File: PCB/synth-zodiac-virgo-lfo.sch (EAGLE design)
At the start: 35 parts, among them Q10 PNP, Q11 NPN, Q9 PNP, U11 TL074A, U12 LM13700

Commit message: Almost ready for FAB.
Sagittarius was mis-spelled, renamed it.  Taurus is still WIP.
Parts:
- removed U11: TL074A, op-amp:QUADTL074A-SOIC
- added U1: TL074A, op-amp:QUADTL074A-SOIC
- PWR: value (none) -> JST, 3P, VT, SMT; device con-jst:04P-VT-SMT -> con-jst:03P-VT-SMT
- renumbered C36 to C1, C39 to C2, C40 to C3, C41 to C4, C42 to C5, OUT_VCF to 2VCF_MOD, OUT_VCO to 2VCO_MOD, Q11 to Q1, R58 to R2, R59 to R3, R60 to R1, R61 to R4, R62 to R5, R63 to R6, R64 to R7, R65 to R8, R66 to R12, R67 to R11, R68 to R10, R69 to R9, U12 to U2
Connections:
- net +9V: now also U1-PWR.V+; no longer U11-PWR.V+
- net -9V: now also U1-PWR.V-; no longer U11-PWR.V-
- net GND: now also PWR.3; no longer PWR.4
- net LFO_OSC: now also U1-D.+; no longer U11-D.+
- net LFO_SQ: now also U1-D.-, U1-D.OUT; no longer U11-D.-, U11-D.OUT
- net LFO_TRI: now also U1-A.-, U1-A.OUT; no longer U11-A.-, U11-A.OUT
- net N$79: now also U1-C.+; no longer U11-C.+
- net N$80: now also U1-C.-, U1-C.OUT; no longer U11-C.-, U11-C.OUT
- net N$85: now also U1-A.+; no longer U11-A.+

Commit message: Work in progress for rev A,  VCO rev.B
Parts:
- removed CP_GND, CP_LFO_CV: PADSMD-070X070, con-testpoints:PADSMD-070X070
- removed WAVE: SPDT, switch-thd:SLIDE-SPDTSS-12-F45-TH-PCB
- added R13: 150K, rlc:RESISTOR0603
- added R14: 47K, rlc:RESISTOR0603
- added R_0-5, R_GND: PADSMD-070X070, con-testpoints:PADSMD-070X070
- added TYPE: (no value), switch-thd:SLIDE-SPDT-MNTSS-12-F45-TH-PCB
- 2VCF_MOD, 2VCO_MOD: value 2-pin, VT, SMT -> JST, SH, 2P; device con-jst:02PVT-SMT -> con-jst:02P-SM-VT-SMT
- PWR: value JST, 3P, VT, SMT -> JST SM 3P; device con-jst:03P-VT-SMT -> con-jst:03P-SM-VT-SMT
- R1: value 221K -> 150K
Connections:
- removed net LFO_CV_IN: CP_LFO_CV.PAD, R1.1
- removed net N$76: R2.1, RATE.2
- new net RATE: R13.1, R2.1, RATE.2
- new net RATE_5: R1.1, R13.2, R14.2, R_0-5.PAD
- net +9V: now also R1.2
- net GND: now also R14.1, R_GND.PAD, U1-B.+, U1-B.-; no longer CP_GND.PAD
- net LFO_CV: now also TYPE-SW.C; no longer WAVE-SW.C
- net LFO_SQ: now also TYPE-SW.B; no longer WAVE-SW.B
- net LFO_TRI: now also TYPE-SW.A; no longer WAVE-SW.A
- net N$77: no longer R1.2
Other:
- note added: "Convert -9 to +9 range to 0-3.3V for LED PCB."
- note added: "SATAN'S CYCLE WORKS"
- note added: "TO LED BOARD"
- note added: "Virgo"
- note added: "Zodiac Synth"
- note removed: "CV_PNL ===>"
- moved on the sheet: 2VCF_MOD, 2VCO_MOD, C1, LED, LFO_SQ, LFO_TRI, PWR, Q1, Q10, Q9, R1, R10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

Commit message: Perhaps final Rev. A?
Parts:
- TYPE: device switch-thd:SLIDE-SPDT-MNTSS-12-F45-TH-PCB -> switch-thd:SLIDE-SPDT-MNTSS-12-F45-TH-PCB-2
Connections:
- net LFO_SQ: now also TYPE-SW.A; no longer TYPE-SW.B
- net LFO_TRI: now also TYPE-SW.B; no longer TYPE-SW.A
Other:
- moved on the sheet: TYPE-SW
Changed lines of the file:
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@@
 <attribute name="REV" value="A"/>
 </part>
-<part name="C1" library="rlc" library_urn="urn:adsk.eagle:library:4192893" deviceset="CAPACITOR" device="0603" package3d_urn="urn:adsk.eagle:package:4193021/4" value="0.1uF"/>
+<part name="C1" library="rlc" library_urn="urn:adsk.eagle:library:4192893" deviceset="CAPACITOR" device="0603" package3d_urn="urn:adsk.eagle:package:4193021/5" value="0.1uF"/>
 <part name="R2" library="rlc" library_urn="urn:adsk.eagle:library:4192893" deviceset="RESISTOR" device="0603" package3d_urn="urn:adsk.eagle:package:4193040/5" value="274K"/>
 <part name="SUPPLY72" library="supply" library_urn="urn:adsk.eagle:library:10485988" deviceset="+9V" device=""/>
@@
 <part name="LED" library="led" library_urn="urn:adsk.eagle:library:5499911" deviceset="SMT" device="0603" package3d_urn="urn:adsk.eagle:package:5499947/3" value="BLU"/>
 <part name="LFO_SQ" library="con-testpoints" library_urn="urn:adsk.eagle:library:7289188" deviceset="TP" device="SMD-040-RND" package3d_urn="urn:adsk.eagle:package:7289200/4" value="TPSMD-040-RND"/>
-<part name="C2" library="rlc" library_urn="urn:adsk.eagle:library:4192893" deviceset="CAPACITOR" device="0603" package3d_urn="urn:adsk.eagle:package:4193021/4" value="0.1uF"/>
-<part name="C3" library="rlc" library_urn="urn:adsk.eagle:library:4192893" deviceset="CAPACITOR" device="0603" package3d_urn="urn:adsk.eagle:package:4193021/4" value="0.1uF"/>
-<part name="C4" library="rlc" library_urn="urn:adsk.eagle:library:4192893" deviceset="CAPACITOR" device="0603" package3d_urn="urn:adsk.eagle:package:4193021/4" value="0.1uF"/>
-<part name="C5" library="rlc" library_urn="urn:adsk.eagle:library:4192893" deviceset="CAPACITOR" device="0603" package3d_urn="urn:adsk.eagle:package:4193021/4" value="0.1uF"/>
+<part name="C2" library="rlc" library_urn="urn:adsk.eagle:library:4192893" deviceset="CAPACITOR" device="0603" package3d_urn="urn:adsk.eagle:package:4193021/5" value="0.1uF"/>
+<part name="C3" library="rlc" library_urn="urn:adsk.eagle:library:4192893" deviceset="CAPACITOR" device="0603" package3d_urn="urn:adsk.eagle:package:4193021/5" value="0.1uF"/>
+<part name="C4" library="rlc" library_urn="urn:adsk.eagle:library:4192893" deviceset="CAPACITOR" device="0603" package3d_urn="urn:adsk.eagle:package:4193021/5" value="0.1uF"/>
+<part name="C5" library="rlc" library_urn="urn:adsk.eagle:library:4192893" deviceset="CAPACITOR" device="0603" package3d_urn="urn:adsk.eagle:package:4193021/5" value="0.1uF"/>
 <part name="SUPPLY94" library="supply" library_urn="urn:adsk.eagle:library:10485988" deviceset="GND" device=""/>
 <part name="SUPPLY95" library="supply" library_urn="urn:adsk.eagle:library:10485988" deviceset="GND" device=""/>
@@
 <part name="PCB1" library="circuit-monkey-zodiac" library_urn="urn:adsk.eagle:library:36060312" deviceset="PENTAGON" device="-40R" package3d_urn="urn:adsk.eagle:package:36376820/2" value="PCB FAB"/>
 <part name="SUPPLY1" library="supply" library_urn="urn:adsk.eagle:library:10485988" deviceset="GND" device=""/>
-<part name="RATE" library="rlc" library_urn="urn:adsk.eagle:library:4192893" deviceset="TRIMPOT" device="9MM_PCB_SHAFT" package3d_urn="urn:adsk.eagle:package:36472483/2" value="10K"/>
+<part name="RATE" library="rlc" library_urn="urn:adsk.eagle:library:4192893" deviceset="TRIMPOT" device="9MM_PCB_SHAFT" package3d_urn="urn:adsk.eagle:package:36472483/3" value="10K"/>
 <part name="SUPPLY2" library="supply" library_urn="urn:adsk.eagle:library:10485988" deviceset="GND" device=""/>
 <part name="SUPPLY3" library="supply" library_urn="urn:adsk.eagle:library:10485988" deviceset="GND" device=""/>
@@
 <part name="SUPPLY6" library="supply" library_urn="urn:adsk.eagle:library:10485988" deviceset="+9V" device=""/>
 <part name="SUPPLY7" library="supply" library_urn="urn:adsk.eagle:library:10485988" deviceset="-9V" device=""/>
-<part name="CONST1" library="circuit-monkey-zodiac" library_urn="urn:adsk.eagle:library:36060312" deviceset="CONSTELLATION" device="-VIRGO" package3d_urn="urn:adsk.eagle:package:36376813/1" value="Virgo"/>
-<part name="GLYPH1" library="circuit-monkey-zodiac" library_urn="urn:adsk.eagle:library:36060312" deviceset="GLYPH" device="-VIRGO" package3d_urn="urn:adsk.eagle:package:36376812/1" value="Virgo"/>
+<part name="CONST1" library="circuit-monkey-zodiac" library_urn="urn:adsk.eagle:library:36060312" deviceset="CONSTELLATION" device="-VIRGO" package3d_urn="urn:adsk.eagle:package:36376813/2" value="Virgo"/>
+<part name="GLYPH1" library="circuit-monkey-zodiac" library_urn="urn:adsk.eagle:library:36060312" deviceset="GLYPH" device="-VIRGO" package3d_urn="urn:adsk.eagle:package:36376812/2" value="Virgo"/>
 <part name="SUPPLY4" library="supply" library_urn="urn:adsk.eagle:library:10485988" deviceset="GND" device=""/>
 <part name="R1" library="rlc" library_urn="urn:adsk.eagle:library:4192893" deviceset="RESISTOR" device="0603" package3d_urn="urn:adsk.eagle:package:4193040/5" value="150K"/>
@@
 <part name="R_0-5" library="con-testpoints" library_urn="urn:adsk.eagle:library:7289188" deviceset="PAD" device="SMD-070X070" package3d_urn="urn:adsk.eagle:package:16261575/3"/>
 <part name="R_GND" library="con-testpoints" library_urn="urn:adsk.eagle:library:7289188" deviceset="PAD" device="SMD-070X070" package3d_urn="urn:adsk.eagle:package:16261575/3"/>
-<part name="TYPE" library="switch-thd" library_urn="urn:adsk.eagle:library:26242324" deviceset="SLIDE-SPDT-MNT" device="SS-12-F45-TH-PCB" package3d_urn="urn:adsk.eagle:package:36475164/3"/>
+<part name="TYPE" library="switch-thd" library_urn="urn:adsk.eagle:library:26242324" deviceset="SLIDE-SPDT-MNT" device="SS-12-F45-TH-PCB-2"/>
 <part name="2VCO_MOD" library="con-jst" library_urn="urn:adsk.eagle:library:7191852" deviceset="02P" device="-SM-VT-SMT" package3d_urn="urn:adsk.eagle:package:41368283/6" value="JST, SH, 2P"/>
 <part name="2VCF_MOD" library="con-jst" library_urn="urn:adsk.eagle:library:7191852" deviceset="02P" device="-SM-VT-SMT" package3d_urn="urn:adsk.eagle:package:41368283/6" value="JST, SH, 2P"/>
@@
 <attribute name="NAME" x="45.974" y="124.46" size="1.27" layer="95" font="vector" ratio="15" align="center-left"/>
 </instance>
-<instance part="TYPE" gate="-SW" x="185.42" y="127" smashed="yes" rot="MR90">
-<attribute name="NAME" x="185.42" y="118.364" size="1.778" layer="95" ratio="15" rot="MR0" align="center"/>
-<attribute name="VALUE" x="191.008" y="127.254" size="0.8128" layer="96" rot="MR90" align="center"/>
+<instance part="TYPE" gate="-SW" x="185.42" y="127" smashed="yes" rot="R270">
+<attribute name="NAME" x="185.42" y="120.396" size="1.778" layer="95" ratio="15" rot="R180" align="center"/>
+<attribute name="VALUE" x="191.008" y="126.746" size="0.8128" layer="96" rot="R270" align="center"/>
 </instance>
 <instance part="2VCO_MOD" gate="G$1" x="220.98" y="134.62" smashed="yes" rot="MR0">
@@
 <wire x1="121.92" y1="101.6" x2="124.46" y2="101.6" width="0.1524" layer="91"/>
 <wire x1="137.16" y1="99.06" x2="139.7" y2="99.06" width="0.1524" layer="91"/>
-<pinref part="TYPE" gate="-SW" pin="A"/>
+<pinref part="TYPE" gate="-SW" pin="B"/>
 </segment>
 </net>
@@
 <pinref part="U1" gate="-D" pin="OUT"/>
 <junction x="167.64" y="129.54"/>
-<pinref part="TYPE" gate="-SW" pin="B"/>
-</segment>
-</net>
+<pinref part="TYPE" gate="-SW" pin="A"/>
+</segment>
+</net>

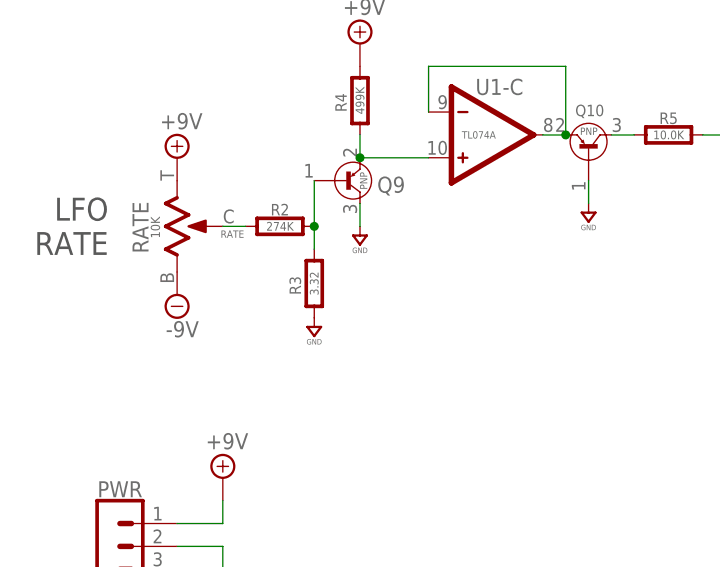
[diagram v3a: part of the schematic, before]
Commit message: Tune values and some schematic visual tweaks.
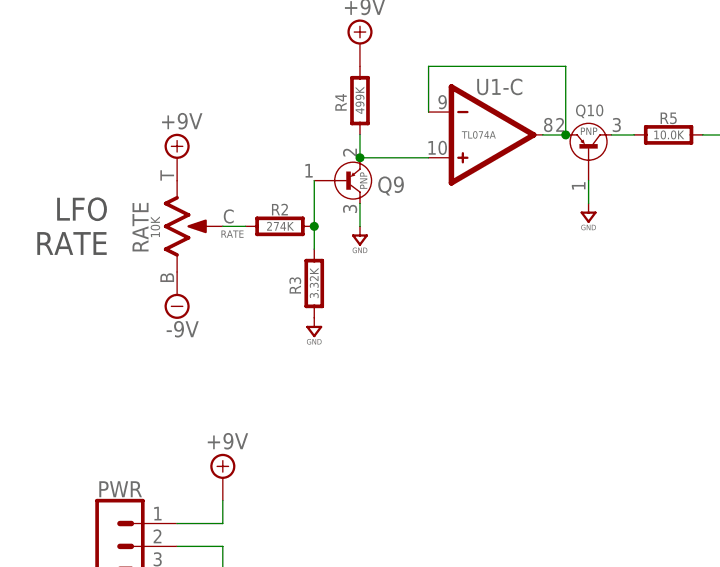
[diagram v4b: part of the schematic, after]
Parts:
- R3: value 3.32 -> 3.32K
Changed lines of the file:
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@@
 <part name="SUPPLY72" library="supply" library_urn="urn:adsk.eagle:library:10485988" deviceset="+9V" device=""/>
 <part name="SUPPLY73" library="supply" library_urn="urn:adsk.eagle:library:10485988" deviceset="-9V" device=""/>
-<part name="R3" library="rlc" library_urn="urn:adsk.eagle:library:4192893" deviceset="RESISTOR" device="0603" package3d_urn="urn:adsk.eagle:package:4193040/5" value="3.32"/>
+<part name="R3" library="rlc" library_urn="urn:adsk.eagle:library:4192893" deviceset="RESISTOR" device="0603" package3d_urn="urn:adsk.eagle:package:4193040/5" value="3.32K"/>
 <part name="SUPPLY74" library="supply" library_urn="urn:adsk.eagle:library:10485988" deviceset="GND" device=""/>
 <part name="Q9" library="transistor-bjt" library_urn="urn:adsk.eagle:library:9359240" deviceset="PNP" device="-BC856" package3d_urn="urn:adsk.eagle:package:9359281/2" value="PNP"/>
